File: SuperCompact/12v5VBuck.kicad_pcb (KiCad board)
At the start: 4 copper layers, 15.4 x 17.3 mm, 16 parts, among them IC1 TPS54302DDCT, J1 Conn_01x02, J2 Conn_01x02

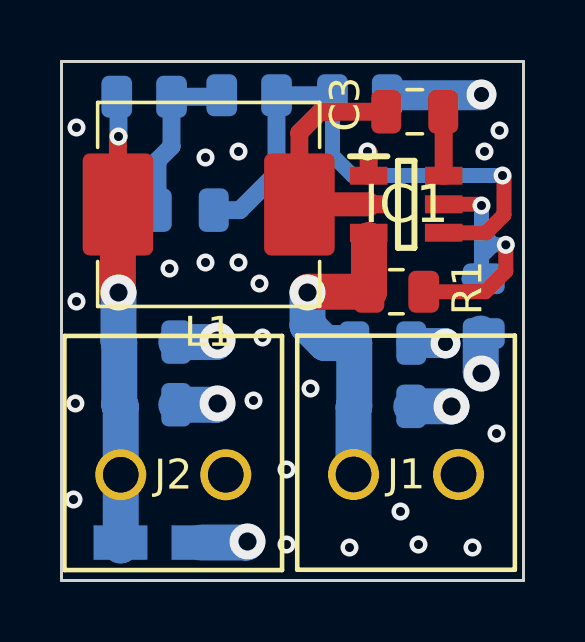
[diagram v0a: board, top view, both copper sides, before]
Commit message: Added bypass capacitor to input
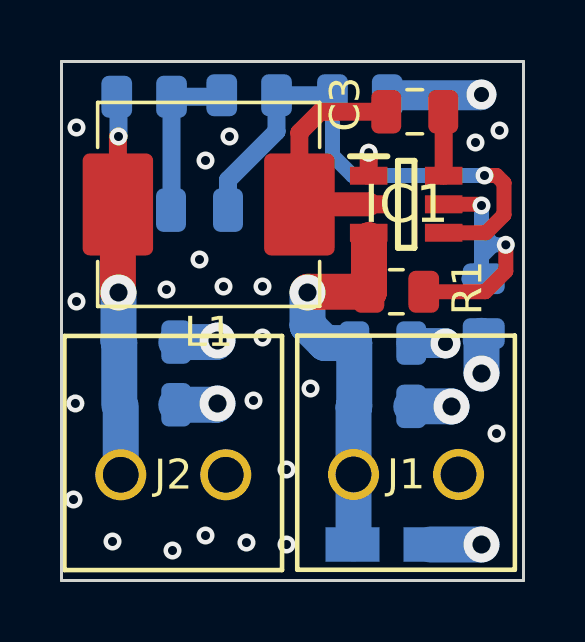
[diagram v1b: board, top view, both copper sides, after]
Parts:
- moved C7 7.74 mm to (66.0, 33.1)
- moved C6 0.48 mm to (59.6, 22.0)
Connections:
- C7 pad 1: +5V -> +12V
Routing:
- net +5V: track 15.0 -> 12.6 mm
- net +12V: track 11.1 -> 13.4 mm
- net Net-(IC1-FB): track 18.6 -> 17.8 mm

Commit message: Added labels
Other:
- board text added: "12V"
- board text added: "5V"
- board text added: "GND"
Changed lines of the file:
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@@
     (pad "2" smd roundrect (at 3.025 0 180) (size 2.35 3.4) (layers "F.Cu" "F.Paste" "F.Mask") (roundrect_rratio 0.1)
       (net 8 "+5V") (pinfunction "2") (pintype "passive"))
-    (model "${KICAD6_3DMODEL_DIR}/Inductor_SMD.3dshapes/L_Abracon_ASPI-0630LR.wrl"
+    (model "${KICAD6_3DMODEL_DIR}/Inductor_SMD.3dshapes/L_Abracon_ASPI-0630LR.wrl" hide
       (offset (xyz 0 0 0))
       (scale (xyz 1 1 1))
@@
       (rotate (xyz 0 0 0))
     )
-    (model "C:/Users/Sylvester Pudelko/Documents/KiCad/7.0/3dmodels/IND_ASPI-0630LR_ABR.step"
+    (model "C:/Users/Sylvester Pudelko/Documents/KiCad/7.0/3dmodels/IND_ASPI-0630LR_ABR.step" hide
+      (offset (xyz 0 0 0))
+      (scale (xyz 1 1 1))
+      (rotate (xyz 0 0 0))
+    )
+    (model "/Users/sylvester/Documents/KiCad/7.0/3dmodels/IND_ASPI-0630LR_ABR.step"
       (offset (xyz 0 0 0))
       (scale (xyz 1 1 1))
@@
   (gr_rect (start 55 17) (end 70.4 34.3)
     (stroke (width 0.1) (type default)) (fill none) (layer "Edge.Cuts"))
+  (gr_text "5V" (at 57.9 33.1) (layer "B.SilkS")
+    (effects (font (size 1 1) (thickness 0.15)) (justify left bottom mirror))
+  )
+  (gr_text "GND" (at 62.1 33) (layer "B.SilkS")
+    (effects (font (size 1 1) (thickness 0.15)) (justify left bottom mirror))
+  )
+  (gr_text "12V" (at 63.5 33.1) (layer "F.SilkS")
+    (effects (font (size 1 1) (thickness 0.15)) (justify left bottom))
+  )
+  (gr_text "GND" (at 66.5 33.1) (layer "F.SilkS")
+    (effects (font (size 1 1) (thickness 0.15)) (justify left bottom))
+  )
+  (gr_text "GND" (at 58.9 33.1) (layer "F.SilkS")
+    (effects (font (size 1 1) (thickness 0.15)) (justify left bottom))
+  )
+  (gr_text "5V" (at 55.9 33.1) (layer "F.SilkS")
+    (effects (font (size 1 1) (thickness 0.15)) (justify left bottom))
+  )
   (segment (start 65.248774 24.675) (end 65.248774 22.96) (width 1.2) (layer "F.Cu") (net 1))
   (segment (start 65.248774 22.96) (end 65.24 22.96) (width 1.2) (layer "F.Cu") (net 1))
@@
   (via (at 61.7 24.5) (size 0.6) (drill 0.3) (layers "F.Cu" "B.Cu") (net 2))
   (via (at 63.3 27.9) (size 0.6) (drill 0.3) (layers "F.Cu" "B.Cu") (net 2))
-  (via (at 61.165 33.035) (size 0.6) (drill 0.3) (layers "F.Cu" "B.Cu") (net 2))
+  (via (at 61.3 33.5) (size 0.6) (drill 0.3) (layers "F.Cu" "B.Cu") (net 2))
   (via (at 69.5 29.4) (size 0.6) (drill 0.3) (layers "F.Cu" "B.Cu") (net 2))
   (via (at 55.5 19.2) (size 0.6) (drill 0.3) (layers "F.Cu" "B.Cu") (net 2))
@@
   (via (at 61.4 28.3) (size 0.6) (drill 0.3) (layers "F.Cu" "B.Cu") (net 2))
   (via (at 68.8 19.7) (size 0.6) (drill 0.3) (layers "F.Cu" "B.Cu") (net 2))
-  (via (at 59.8 32.8) (size 0.6) (drill 0.3) (layers "F.Cu" "B.Cu") (net 2))
-  (via (at 56.7 33) (size 0.6) (drill 0.3) (layers "F.Cu" "B.Cu") (net 2))
+  (via (at 59.8 33.4) (size 0.6) (drill 0.3) (layers "F.Cu" "B.Cu") (net 2))
+  (via (at 57 33.4) (size 0.6) (drill 0.3) (layers "F.Cu" "B.Cu") (net 2))
   (via (at 60.4 24.5) (size 0.6) (drill 0.3) (layers "F.Cu" "B.Cu") (net 2))
   (via (at 60.6 19.5) (size 0.6) (drill 0.3) (layers "F.Cu" "B.Cu") (net 2))
@@
   (via (at 68 28.5) (size 1.2) (drill 0.6) (layers "F.Cu" "B.Cu") (net 2))
   (via (at 69.6 19.3) (size 0.6) (drill 0.3) (layers "F.Cu" "B.Cu") (net 2))
-  (via (at 55.4 31.6) (size 0.6) (drill 0.3) (layers "F.Cu" "B.Cu") (net 2))
-  (via (at 58.7 33.3) (size 0.6) (drill 0.3) (layers "F.Cu" "B.Cu") (net 2))
+  (via (at 55.6 32.1) (size 0.6) (drill 0.3) (layers "F.Cu" "B.Cu") (net 2))
+  (via (at 58.5 32.5) (size 0.6) (drill 0.3) (layers "F.Cu" "B.Cu") (net 2))
   (via (at 69 27.4) (size 1.2) (drill 0.6) (layers "F.Cu" "B.Cu") (net 2))
   (segment (start 67.3 33.1) (end 69 33.1) (width 1.2) (layer "B.Cu") (net 2))
